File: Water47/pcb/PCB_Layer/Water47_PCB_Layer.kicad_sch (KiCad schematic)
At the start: 104 parts, among them SW1 Esc, SW10 O, SW11 P, SW12 -, SW13 Del, SW14 Cmd, SW15 A, SW16 S, SW17 D, SW18 F, SW19 G, SW2 Q, SW20 H, SW21 J, SW22 K, SW23 L, SW24 ;, SW25 Bs, SW26 Shift(L), SW27 Z, SW28 X, SW29 C, SW3 W, SW30 V, SW31 B, SW32 N, SW33 M, SW34 ,, SW35 ., SW36 Shift(R), SW37 Fn, SW38 Ctrl(L), SW39 Win(L), SW4 E, SW40 Alt(L), SW41 Shift(C), SW42 Fn(C), SW43 Enter, SW44 ←, SW45 ↓, SW46 ↑, SW47 →, SW5 R, SW6 T, SW7 Y, SW8 U, SW9 I, U1 MOUDLE-SEEEDUINO-XIAO

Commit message: feat: first wiring
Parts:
- SW1, SW10, SW11, SW12, SW13, SW15, SW16, SW17, SW18, SW19, SW2, SW20, SW21, SW22, SW23, SW24, SW27, SW28, SW29, SW3, SW30, SW31, SW32, SW33, SW34, SW35, SW37, SW4, SW44, SW45, SW46, SW47, SW5, SW6, SW7, SW8, SW9: footprint multifeb13_kbd_KiCad_lib:Kailh_Choc_V1_Hotswap_via_1u -> multifeb13_kbd_KiCad_lib:Kailh_Choc_V2_1u_wo_anker
- SW14, SW36, SW38, SW39, SW40, SW42: footprint multifeb13_kbd_KiCad_lib:Kailh_Choc_V1_Hotswap_via_1.25u -> multifeb13_kbd_KiCad_lib:Kailh_Choc_V2_1.25u_wo_anker
- SW25, SW26: footprint multifeb13_kbd_KiCad_lib:Kailh_Choc_V1_Hotswap_via_1.75u -> multifeb13_kbd_KiCad_lib:Kailh_Choc_V2_1.75u_wo_anker
- SW41, SW43: footprint multifeb13_kbd_KiCad_lib:Kailh_Choc_V1_Hotswap_via_2u -> multifeb13_kbd_KiCad_lib:Kailh_Choc_V2_2u_wo_anker
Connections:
- net PIN2: now also U1.9 (PA7_A8_D8_SCK); no longer U1.2 (PA4_A1_D1)
- net PIN3: now also U1.4 (PA11_A3_D3); no longer U1.3 (PA10_A2_D2)
- net PIN4: now also U1.11 (PA6_A10_D10_MOSI); no longer U1.4 (PA11_A3_D3)
- net PIN5: now also U1.3 (PA10_A2_D2); no longer U1.7 (PB08_A6_D6_TX)
- net PIN6: now also U1.10 (PA5_A9_D9_MISO); no longer U1.11 (PA6_A10_D10_MOSI)
- net PIN7: now also U1.8 (PB09_A7_D7_RX); no longer U1.10 (PA5_A9_D9_MISO)
- net PIN8: now also U1.7 (PB08_A6_D6_TX); no longer U1.9 (PA7_A8_D8_SCK)

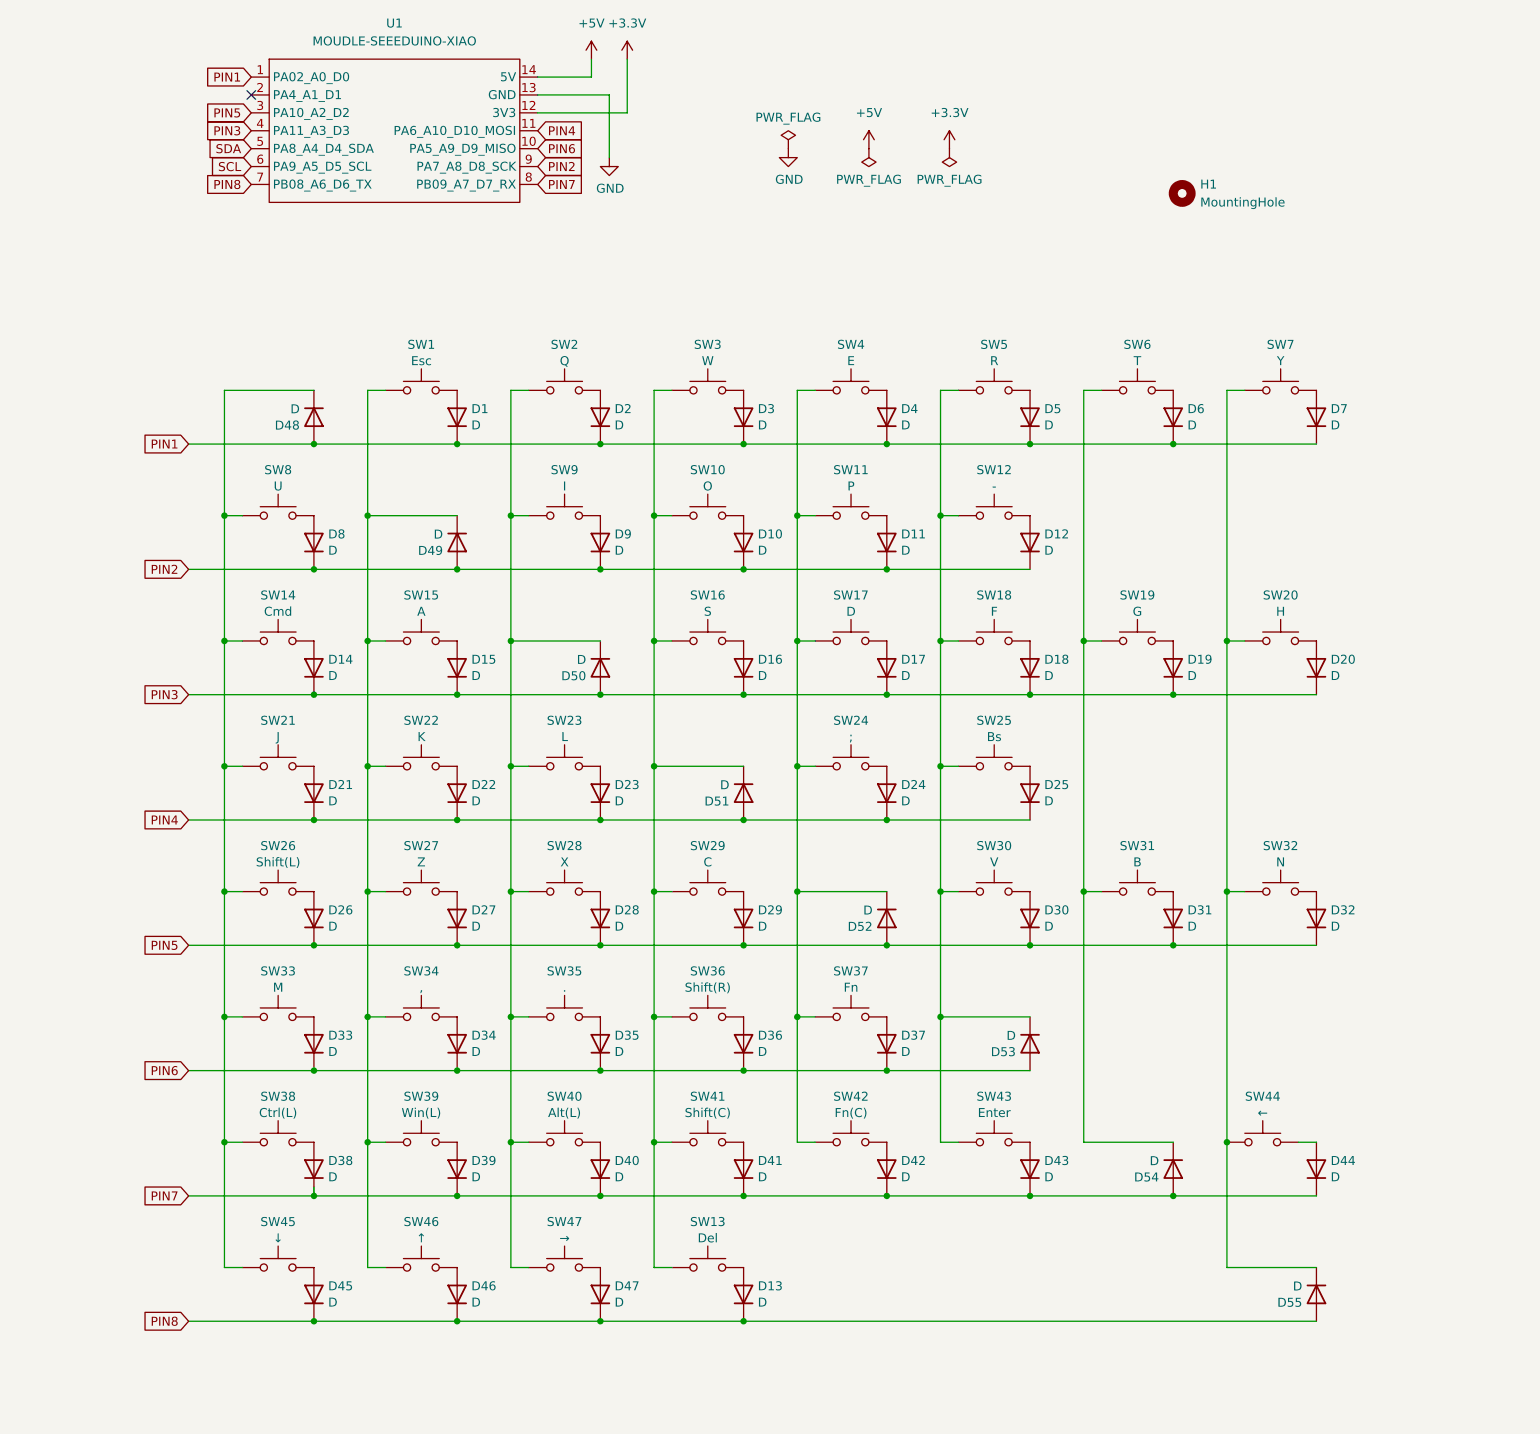
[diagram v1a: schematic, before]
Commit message: feat: add symbol, annotating
add MoutingHoles
update annotating
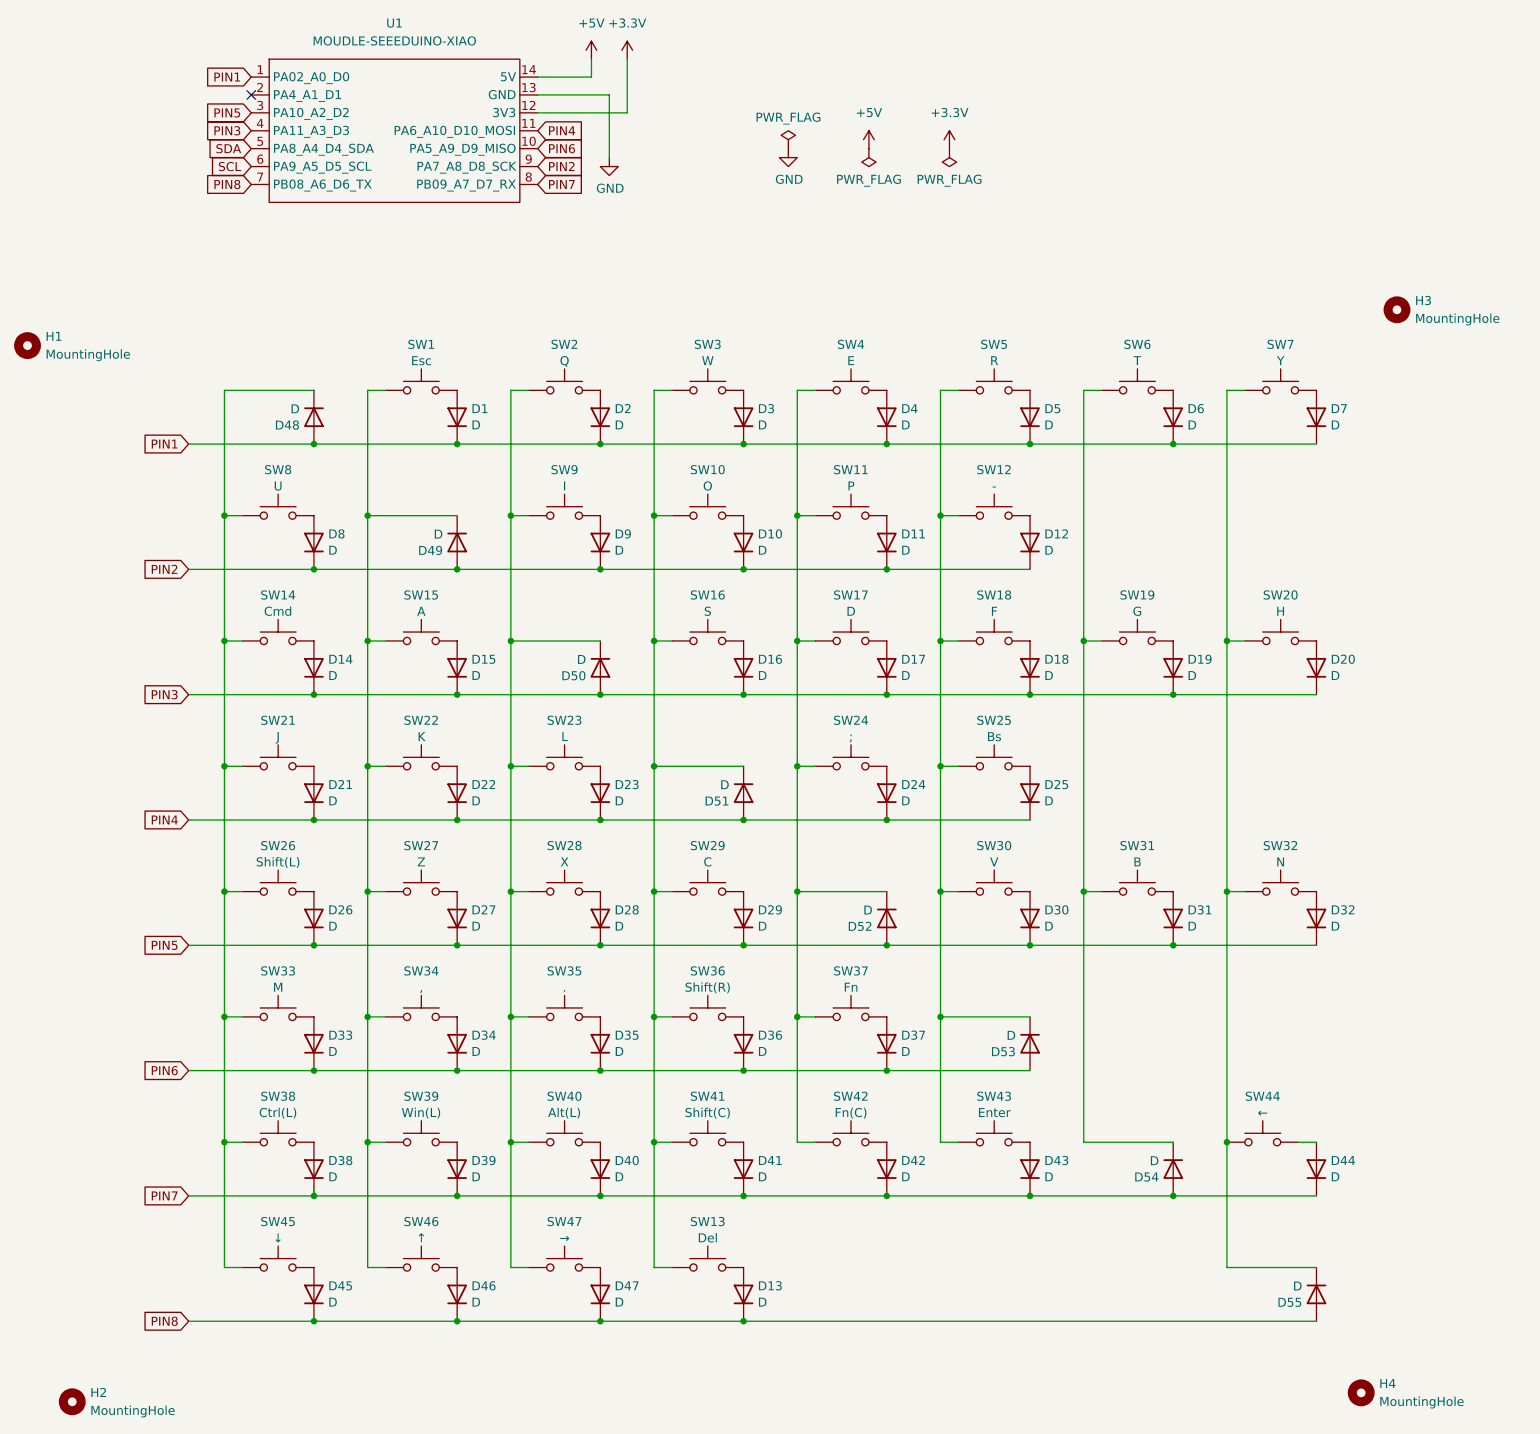
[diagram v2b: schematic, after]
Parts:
- added H2, H3, H4: MountingHole, kbd_Hole:m2_Screw_Hole, symbol Mechanical:MountingHole
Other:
- moved on the sheet: H1

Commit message: feat: change key layout
2u -> 1.75u to not put stabilizer
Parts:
- SW40: footprint multifeb13_kbd_KiCad_lib:Kailh_Choc_V2_1.25u_wo_anker -> multifeb13_kbd_KiCad_lib:Kailh_Choc_V2_1.5u_wo_anker
- SW41, SW43: footprint multifeb13_kbd_KiCad_lib:Kailh_Choc_V2_2u_wo_anker -> multifeb13_kbd_KiCad_lib:Kailh_Choc_V2_1.75u_wo_anker
- SW44: footprint multifeb13_kbd_KiCad_lib:Kailh_Choc_V2_1u_wo_anker -> multifeb13_kbd_KiCad_lib:Kailh_Choc_V2_1.25u_wo_anker
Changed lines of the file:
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@@
     (property "Reference" "SW40" (id 0) (at 99.06 175.133 0))
     (property "Value" "Alt(L)" (id 1) (at 99.06 177.4444 0))
-    (property "Footprint" "multifeb13_kbd_KiCad_lib:Kailh_Choc_V2_1.25u_wo_anker" (id 2) (at 99.06 176.53 0)
+    (property "Footprint" "multifeb13_kbd_KiCad_lib:Kailh_Choc_V2_1.5u_wo_anker" (id 2) (at 99.06 176.53 0)
       (effects (font (size 1.27 1.27)) hide)
     )
@@
     (property "Reference" "SW41" (id 0) (at 119.38 175.133 0))
     (property "Value" "Shift(C)" (id 1) (at 119.38 177.4444 0))
-    (property "Footprint" "multifeb13_kbd_KiCad_lib:Kailh_Choc_V2_2u_wo_anker" (id 2) (at 119.38 176.53 0)
+    (property "Footprint" "multifeb13_kbd_KiCad_lib:Kailh_Choc_V2_1.75u_wo_anker" (id 2) (at 119.38 176.53 0)
       (effects (font (size 1.27 1.27)) hide)
     )
@@
     (property "Reference" "SW43" (id 0) (at 160.02 175.133 0))
     (property "Value" "Enter" (id 1) (at 160.02 177.4444 0))
-    (property "Footprint" "multifeb13_kbd_KiCad_lib:Kailh_Choc_V2_2u_wo_anker" (id 2) (at 160.02 176.53 0)
+    (property "Footprint" "multifeb13_kbd_KiCad_lib:Kailh_Choc_V2_1.75u_wo_anker" (id 2) (at 160.02 176.53 0)
       (effects (font (size 1.27 1.27)) hide)
     )
@@
     (property "Reference" "SW44" (id 0) (at 198.12 175.133 0))
     (property "Value" "←" (id 1) (at 198.12 177.4444 0))
-    (property "Footprint" "multifeb13_kbd_KiCad_lib:Kailh_Choc_V2_1u_wo_anker" (id 2) (at 198.12 176.53 0)
+    (property "Footprint" "multifeb13_kbd_KiCad_lib:Kailh_Choc_V2_1.25u_wo_anker" (id 2) (at 198.12 176.53 0)
       (effects (font (size 1.27 1.27)) hide)
     )
@@
     )
     (path "/4aa4644f-18e3-4962-ba5d-249e3f9e24b0"
-      (reference "SW40") (unit 1) (value "Alt(L)") (footprint "multifeb13_kbd_KiCad_lib:Kailh_Choc_V2_1.25u_wo_anker")
+      (reference "SW40") (unit 1) (value "Alt(L)") (footprint "multifeb13_kbd_KiCad_lib:Kailh_Choc_V2_1.5u_wo_anker")
     )
     (path "/534da0b5-be60-4e98-9fd4-84ec0df6de7f"
-      (reference "SW41") (unit 1) (value "Shift(C)") (footprint "multifeb13_kbd_KiCad_lib:Kailh_Choc_V2_2u_wo_anker")
+      (reference "SW41") (unit 1) (value "Shift(C)") (footprint "multifeb13_kbd_KiCad_lib:Kailh_Choc_V2_1.75u_wo_anker")
     )
     (path "/561b7eb2-183e-43c1-a564-c265b8f3c76f"
@@
     )
     (path "/7f68f2f9-1a40-4e2d-bda1-32170086ae6f"
-      (reference "SW43") (unit 1) (value "Enter") (footprint "multifeb13_kbd_KiCad_lib:Kailh_Choc_V2_2u_wo_anker")
+      (reference "SW43") (unit 1) (value "Enter") (footprint "multifeb13_kbd_KiCad_lib:Kailh_Choc_V2_1.75u_wo_anker")
     )
     (path "/d5a950b8-c579-4504-be73-5424804140b0"
-      (reference "SW44") (unit 1) (value "←") (footprint "multifeb13_kbd_KiCad_lib:Kailh_Choc_V2_1u_wo_anker")
+      (reference "SW44") (unit 1) (value "←") (footprint "multifeb13_kbd_KiCad_lib:Kailh_Choc_V2_1.25u_wo_anker")
     )
     (path "/5b1126e5-75d1-4c04-9289-bc0ec07f3a86"
